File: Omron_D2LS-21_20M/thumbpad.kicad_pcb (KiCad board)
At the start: 2 copper layers, 34 x 34 mm, 15 parts, among them J1 Conn_01x10, SW1 D2LS-2120M, SW2 D2LS-2120M, SW3 D2LS-2120M, SW4 D2LS-2120M, U1 MAX6817, U2 MAX6817

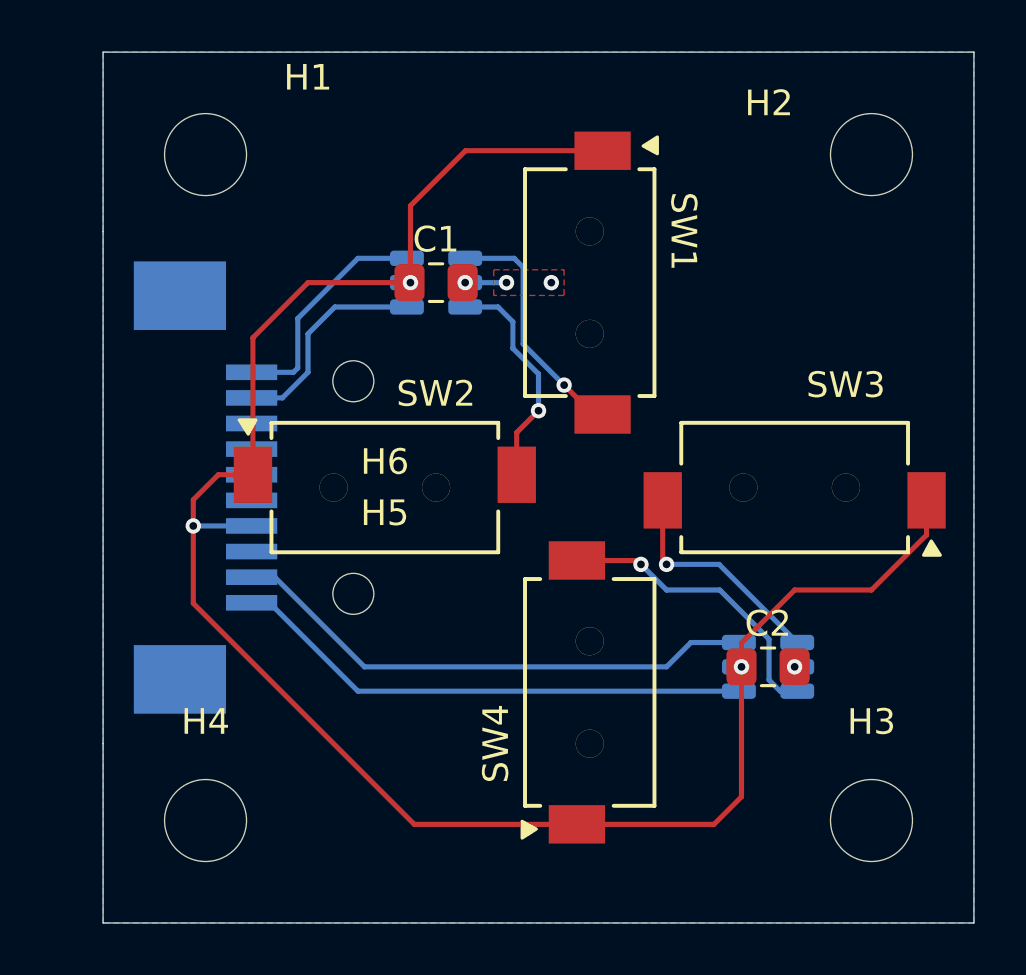
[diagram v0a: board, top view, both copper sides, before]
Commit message: 6pos connector added, board shrink
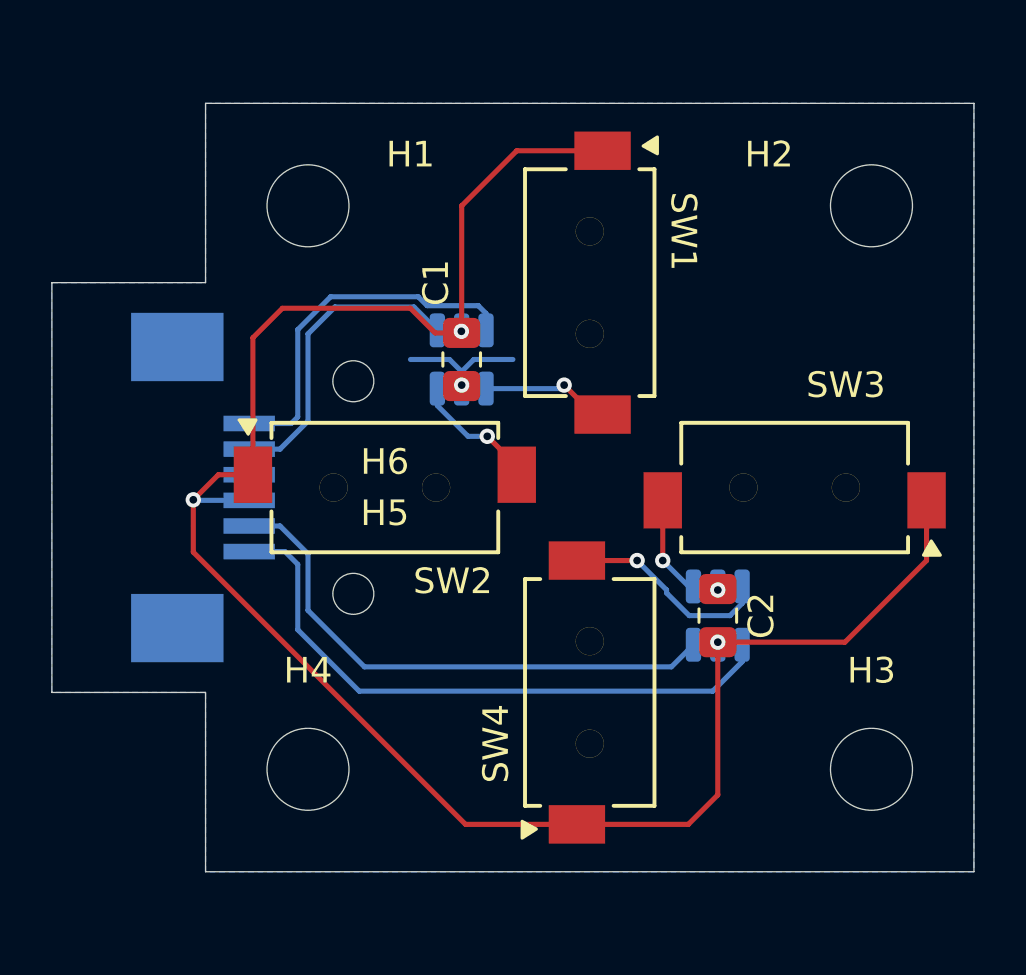
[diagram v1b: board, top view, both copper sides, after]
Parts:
- J1: value Conn_01x10 -> Conn_01x06; footprint Connector_FFC-FPC:TE_1-84952-0_1x10-1MP_P1.0mm_Horizontal -> My_Library:TEAmp-CON6-84953-SMT-RA-FCC-FPC
- moved H1 4.47 mm to (139.0, 69.0)
- moved H4 4.47 mm to (139.0, 91.0)
- moved C1 3.16 mm to (145.0, 75.0), turned to -90 degrees
- moved U1 3.16 mm to (145.0, 75.0), turned to 90 degrees
- moved C2 2.80 mm to (155.0, 85.0), turned to 90 degrees
- moved U2 2.80 mm to (155.0, 85.0), turned to -90 degrees
- moved H2 2.00 mm to (161.0, 69.0)
- moved H3 2.00 mm to (161.0, 91.0)
- moved J1 1.00 mm to (134.0, 80.0), turned to -90 degrees
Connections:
- J1 pad 3: unconnected-(J1-Pin_3-Pad3) -> +5V
- J1 pad 4: +5V -> GND
- J1 pad 5: unconnected-(J1-Pin_5-Pad5) -> U1O2_2
- J1 pad 6: GND -> U1O1_1
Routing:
- net U1O1_1: track 9.04 -> 14.2 mm
- net Net-(SW3-NO): track 8.93 -> 3.97 mm
- net Net-(SW1-NO): track 9.65 -> 5.08 mm
- net Net-(SW2-NO): track 9.05 -> 5.09 mm
- net U2O2_4: track 20.5 -> 24.1 mm
- net U1O2_2: track 8.41 -> 12.0 mm
- net Net-(SW4-NO): track 11.6 -> 8.27 mm
- net GND: track 1.81 -> 5.06 mm, vias 4 -> 2
- net +5V: track 75.0 -> 76.3 mm
- removed copper zone on F.Cu, net GND
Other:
- board size 34 x 34 mm -> 36 x 30 mm

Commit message: board shrunk/final shape v1
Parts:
- moved H5 7.87 mm to (141.8, 76.3)
- moved H6 7.87 mm to (141.8, 83.7)
- moved U1 3.16 mm to (144.0, 72.0)
- moved C1 3.13 mm to (144.0, 72.0)
- moved U2 2.24 mm to (156.0, 87.0)
- moved C2 2.20 mm to (156.0, 87.0)
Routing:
- net +5V: track 76.3 -> 70.3 mm, vias 3 -> 2
- net GND: track 5.06 -> 0.00 mm, vias 2 -> 1
- net Net-(SW2-NO): track 5.09 -> 9.27 mm
- net Net-(SW1-NO): track 5.08 -> 8.47 mm
- net Net-(SW4-NO): track 8.27 -> 10.7 mm
- net Net-(SW3-NO): track 3.97 -> 6.27 mm
- net U2O2_4: track 24.1 -> 26.2 mm
- net U2O1_3: track 21.3 -> 22.4 mm
- net U1O2_2: track 12.0 -> 11.5 mm

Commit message: Added jumpers to bypass debouncers
Debouncing ICs are expensive, allows for software debounce option
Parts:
- added JP1: Jumper_2_Small_Open, Jumper:SolderJumper-2_P1.3mm_Open_Pad1.0x1.5mm, F.Cu at (155.0, 70.3)
- added JP2: Jumper_2_Small_Open, Jumper:SolderJumper-2_P1.3mm_Open_Pad1.0x1.5mm, F.Cu at (155.0, 74.3)
- added JP3: Jumper_2_Small_Open, Jumper:SolderJumper-2_P1.3mm_Open_Pad1.0x1.5mm, F.Cu at (145.0, 85.7)
- added JP4: Jumper_2_Small_Open, Jumper:SolderJumper-2_P1.3mm_Open_Pad1.0x1.5mm, F.Cu at (145.0, 89.3)
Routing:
- net U1O2_2: track 11.5 -> 25.0 mm, vias 0 -> 1
- net U1O1_1: track 14.0 -> 25.9 mm, vias 0 -> 1
- net Net-(JP3-A): track 6.27 -> 16.6 mm
- net Net-(JP2-A): track 9.27 -> 19.6 mm
- net Net-(JP4-A): track 10.7 -> 20.8 mm
- net Net-(JP1-A): track 8.47 -> 17.7 mm
- net U2O2_4: track 26.2 -> 30.5 mm, vias 0 -> 1
- net U2O1_3: track 22.4 -> 26.5 mm, vias 0 -> 1
